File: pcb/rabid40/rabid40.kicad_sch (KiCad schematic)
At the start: 12 parts

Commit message: schematic basics laid down
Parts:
- added D1, D2, D3, D4: 1N4148W, Diode_SMD:D_SOD-123, symbol Diode:1N4148W
- added F1: 500mA, Fuse:Fuse_1206_3216Metric, symbol Device:Polyfuse_Small
- added MX1, MX2, MX3, MX4: MX-NoLED, MX_Alps_Hybrid:MX-1U-NoLED, symbol ai03-mx-alps-hybrid:MX-NoLED
- added R3: 10k, Resistor_SMD:R_0805_2012Metric, symbol Device:R_Small
- added SW1: SW_PUSH, random-keyboard-parts:SKQG-1155865, symbol Keyboard_Symbols:SW_PUSH
- added USB1: Molex-0548190589, random-keyboard-parts:Molex-0548190589, symbol ai03-random-parts:Molex-0548190589
- C1, C2, C3, C4, C5, C6, C7: renamed from C?; footprint (none) -> Capacitor_SMD:C_0805_2012Metric
- R1, R2, R4: renamed from R?; footprint (none) -> Resistor_SMD:R_0805_2012Metric
- Y1: renamed from Y?; footprint (none) -> Crystal:Crystal_SMD_3225-4Pin_3.2x2.5mm
- gave numbers to parts that had none: 1
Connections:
- net +5V: now also F1.2, R3.2
- net GND: now also SW1.1, USB1.1 (GND)
- net D+: now reaches R2.1
- net D+: now also USB1.3 (D+)
- net at U1.13 (~{RESET}): now also R3.1, SW1.2
- net D-: now reaches R1.1
- net D-: now also USB1.4 (D-)
- new net: D2.2 (A), MX2.2 (ROW)
- new net: D4.2 (A), MX4.2 (ROW)
- new net: D1.2 (A), MX1.2 (ROW)
- new net: D3.2 (A), MX3.2 (ROW)
- new net Col0: MX1.1 (COL), MX2.1 (COL)
- new net Col1: MX3.1 (COL), MX4.1 (COL)
- new net Row0: D1.1 (K), D2.1 (K), D3.1 (K), D4.1 (K)
- new net VCC: F1.1, USB1.5 (VBUS)
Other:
- moved on the sheet: C1, C2, C3, C4, C5, C6, C7, R1, R2, R4, U1, Y1

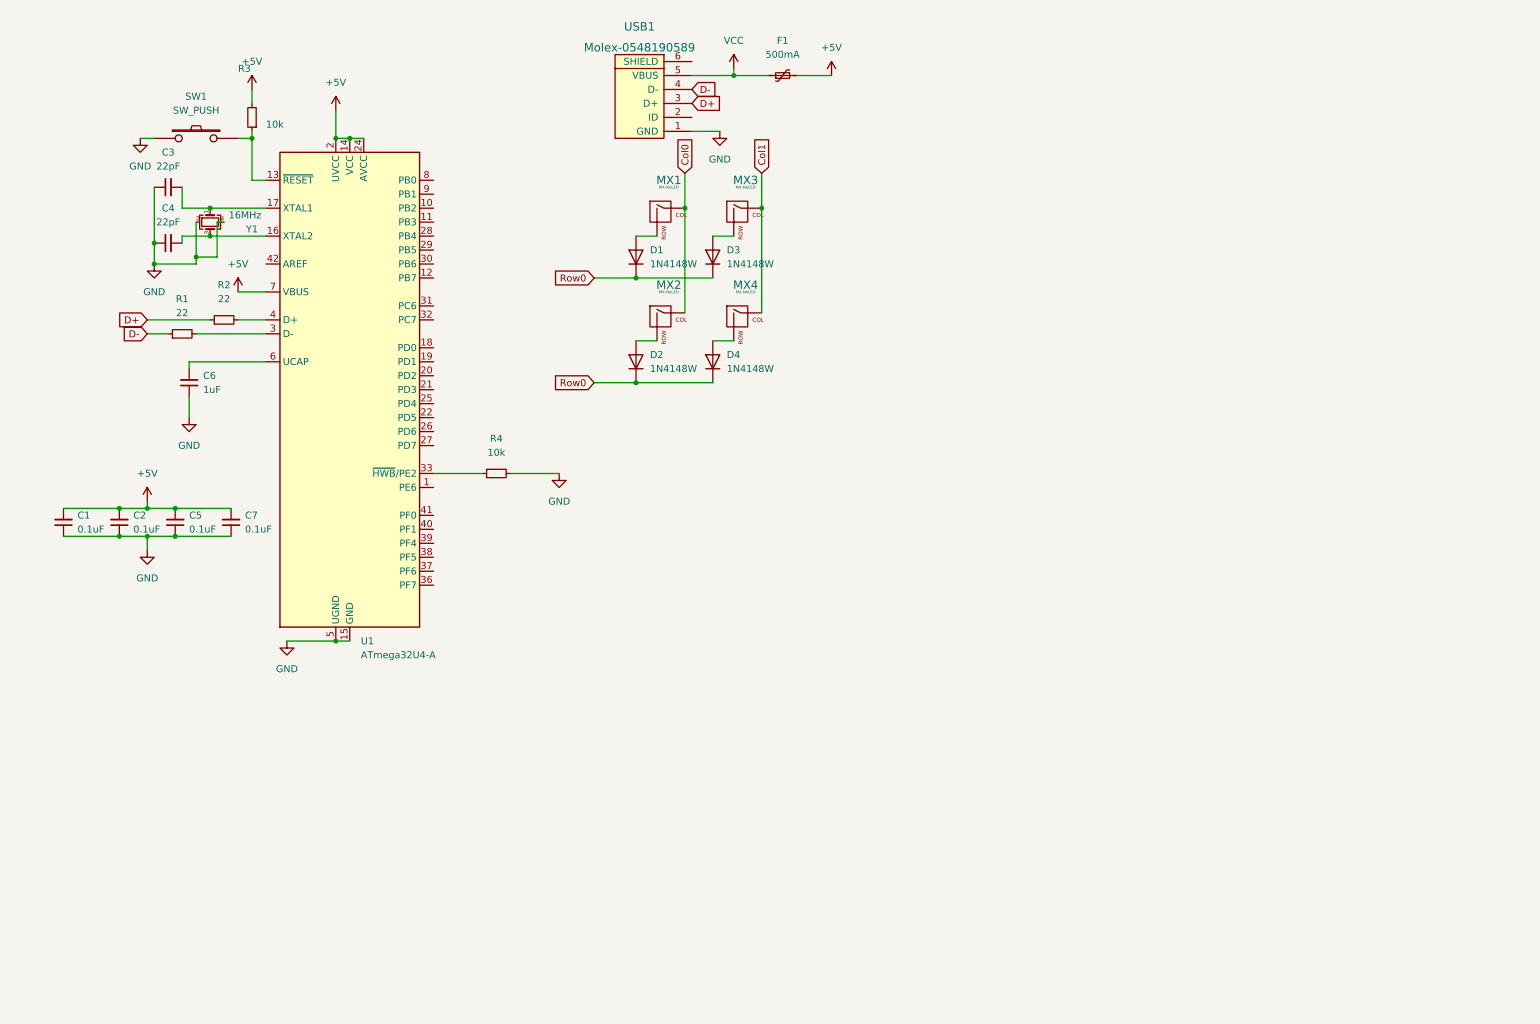
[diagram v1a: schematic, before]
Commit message: all components added for the 40
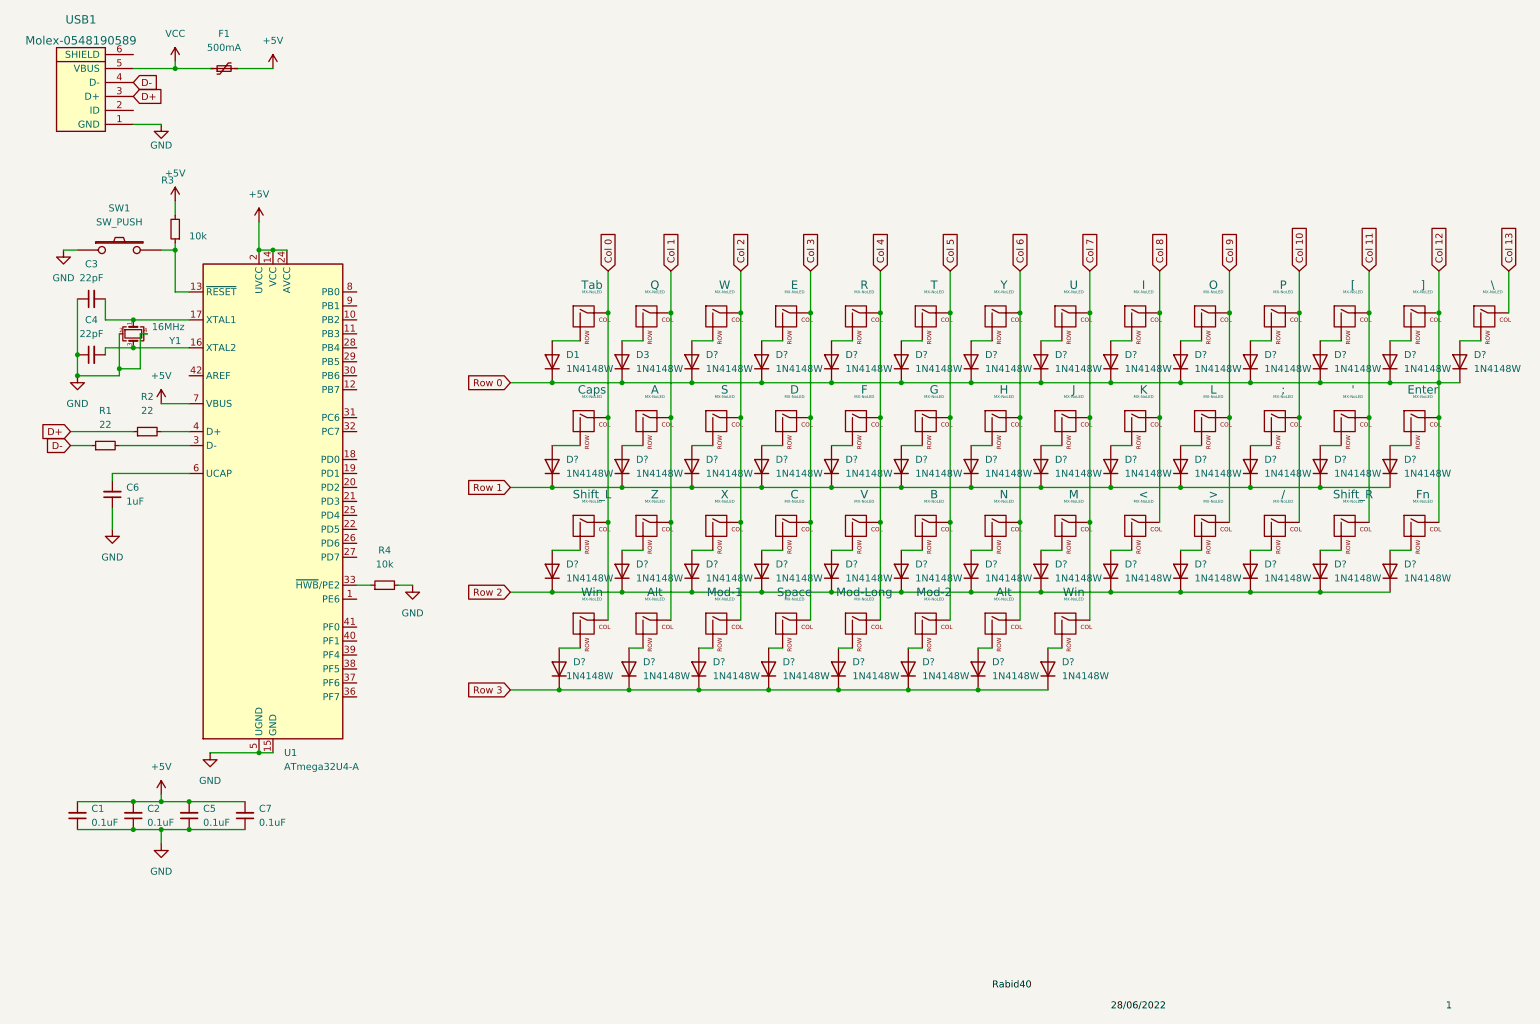
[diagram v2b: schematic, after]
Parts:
- removed D2, D4: 1N4148W, Diode_SMD:D_SOD-123, symbol Diode:1N4148W
- removed MX2, MX4: MX-NoLED, MX_Alps_Hybrid:MX-1U-NoLED, symbol ai03-mx-alps-hybrid:MX-NoLED
- added ', /, ;, <, >, A, Alt (x2), B, C, Caps, D, E, Enter, F, Fn, G, H, I, J, K, L, M, Mod-1, Mod-2, Mod-Long, N, O, P, R, S, Shift_L, Shift_R, Space, T, U, V, W, Win (x2), X, Y, Z, [, \, ]: MX-NoLED, MX_Alps_Hybrid:MX-1U-NoLED, symbol ai03-mx-alps-hybrid:MX-NoLED
- added D? (x46): 1N4148W, Diode_SMD:D_SOD-123, symbol Diode:1N4148W
- renumbered MX3 to Q, MX1 to Tab
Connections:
- net Col0 renamed Col 0
- net Col 0: now also Caps.1 (COL), Shift_L.1 (COL), Win.1 (COL)
- net Col1 renamed Col 1
- net Col 1: now also A.1 (COL), Alt.1 (COL), Z.1 (COL)
- net Row0 renamed Col 12
- net Col 12: now also D?.1 (K), D?.1 (K), D?.1 (K), D?.1 (K), D?.1 (K), D?.1 (K), D?.1 (K), D?.1 (K), D?.1 (K), D?.1 (K), D?.1 (K), D?.1 (K), Enter.1 (COL), Fn.1 (COL), ].1 (COL)
- new net: D?.2 (A), Y.2 (ROW)
- new net: D?.2 (A), U.2 (ROW)
- new net: <.2 (ROW), D?.2 (A)
- new net: D?.2 (A), W.2 (ROW)
- new net: D?.2 (A), G.2 (ROW)
- new net: D?.2 (A), K.2 (ROW)
- new net: D?.2 (A), T.2 (ROW)
- new net: D?.2 (A), P.2 (ROW)
- new net: D?.2 (A), X.2 (ROW)
- new net: B.2 (ROW), D?.2 (A)
- new net: D?.2 (A), J.2 (ROW)
- new net: D?.2 (A), O.2 (ROW)
- new net: A.2 (ROW), D?.2 (A)
- new net: ;.2 (ROW), D?.2 (A)
- new net: D?.2 (A), ].2 (ROW)
- new net: D?.2 (A), E.2 (ROW)
- new net: >.2 (ROW), D?.2 (A)
- new net: Alt.2 (ROW), D?.2 (A) (x2)
- new net: D?.2 (A), Mod-1.2 (ROW)
- new net: D?.2 (A), V.2 (ROW)
- new net: D?.2 (A), M.2 (ROW)
- new net: D?.2 (A), Enter.2 (ROW)
- new net: D?.2 (A), I.2 (ROW)
- new net: D?.2 (A), S.2 (ROW)
- new net: D?.2 (A), Fn.2 (ROW)
- new net: D?.2 (A), [.2 (ROW)
- new net: D?.2 (A), L.2 (ROW)
- new net: D?.2 (A), Z.2 (ROW)
- new net: D?.2 (A), Win.2 (ROW) (x2)
- new net: '.2 (ROW), D?.2 (A)
- new net: Caps.2 (ROW), D?.2 (A)
- new net: /.2 (ROW), D?.2 (A)
- new net: D?.2 (A), \.2 (ROW)
- new net: D?.2 (A), Space.2 (ROW)
- new net: D?.2 (A), Mod-2.2 (ROW)
- new net: C.2 (ROW), D?.2 (A)
- new net: D?.2 (A), R.2 (ROW)
- new net: D.2 (ROW), D?.2 (A)
- new net: D?.2 (A), F.2 (ROW)
- new net: D?.2 (A), N.2 (ROW)
- new net: D?.2 (A), Shift_R.2 (ROW)
- new net: D?.2 (A), Shift_L.2 (ROW)
- new net: D?.2 (A), H.2 (ROW)
- new net: D?.2 (A), Mod-Long.2 (ROW)
- new net Col 10: /.1 (COL), ;.1 (COL), P.1 (COL)
- new net Col 11: '.1 (COL), Shift_R.1 (COL), [.1 (COL)
- new net Col 13: \.1 (COL)
- new net Col 2: Mod-1.1 (COL), S.1 (COL), W.1 (COL), X.1 (COL)
- new net Col 3: C.1 (COL), D.1 (COL), E.1 (COL), Space.1 (COL)
- new net Col 4: F.1 (COL), Mod-Long.1 (COL), R.1 (COL), V.1 (COL)
- new net Col 5: B.1 (COL), G.1 (COL), Mod-2.1 (COL), T.1 (COL)
- new net Col 6: Alt.1 (COL), H.1 (COL), N.1 (COL), Y.1 (COL)
- new net Col 7: J.1 (COL), M.1 (COL), U.1 (COL), Win.1 (COL)
- new net Col 8: <.1 (COL), I.1 (COL), K.1 (COL)
- new net Col 9: >.1 (COL), L.1 (COL), O.1 (COL)
- new net Row 1: D?.1 (K), D?.1 (K), D?.1 (K), D?.1 (K), D?.1 (K), D?.1 (K), D?.1 (K), D?.1 (K), D?.1 (K), D?.1 (K), D?.1 (K), D?.1 (K), D?.1 (K)
- new net Row 2: D?.1 (K), D?.1 (K), D?.1 (K), D?.1 (K), D?.1 (K), D?.1 (K), D?.1 (K), D?.1 (K), D?.1 (K), D?.1 (K), D?.1 (K), D?.1 (K), D?.1 (K)
- new net Row 3: D?.1 (K), D?.1 (K), D?.1 (K), D?.1 (K), D?.1 (K), D?.1 (K), D?.1 (K), D?.1 (K)
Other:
- moved on the sheet: C1, C2, C3, C4, C5, C6, C7, D1, D3, F1, Q, R1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

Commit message: basic routing
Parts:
- Caps1: renamed from Caps; footprint MX_Alps_Hybrid:MX-1U-NoLED -> MX_Alps_Hybrid:MX-1.25U
- gave numbers to parts that had none: 46
- renumbered ' to '1, / to /1, ; to ;1, < to <1, > to >1, A to A1, Alt to Alt1, Alt to Alt2, B to B1, C to C8, D to D17, E to E1, Enter to Enter1, F to F2, Fn to Fn1, G to G1, H to H1, I to I1, J to J1, K to K1, L to L1, M to M1, Mod-Long to Mod-Long1, N to N1, O to O1, P to P1, Q to Q1, R to R5, S to S1, Shift_L to Shift_L1, Shift_R to Shift_R1, Space to Space1, T to T1, Tab to Tab1, U to U2, V to V1, W to W1, Win to Win1, Win to Win2, X to X1, Y to Y2, Z to Z1, [ to [1, \ to \1, ] to ]1

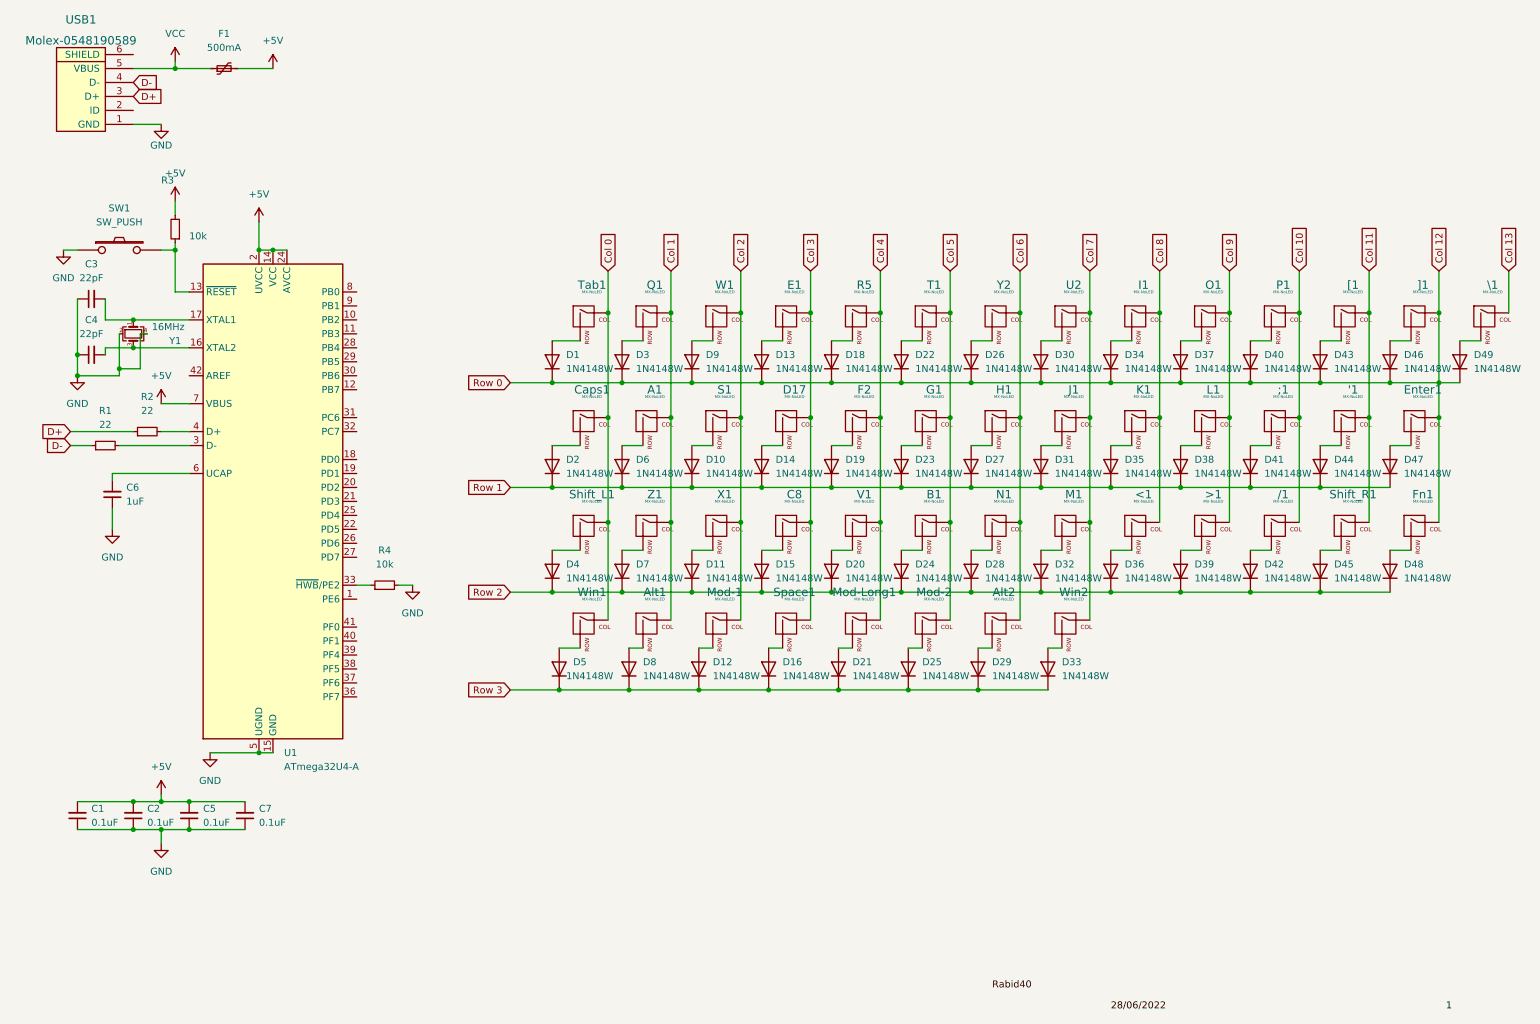
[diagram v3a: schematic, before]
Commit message: added multilayout support to schematic
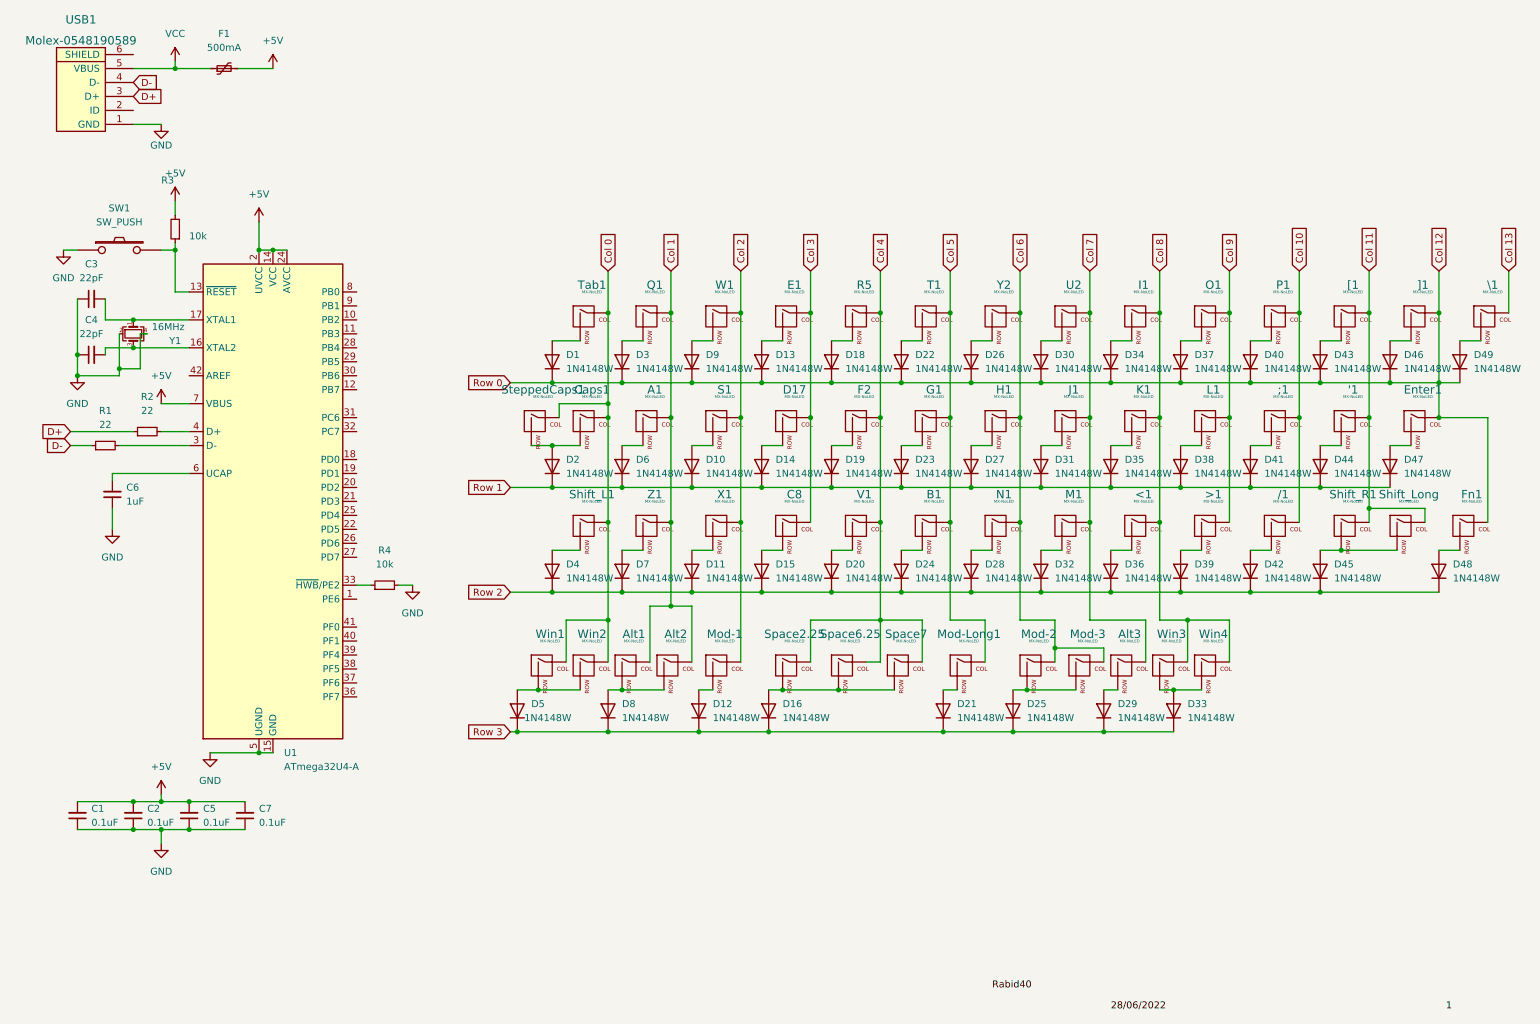
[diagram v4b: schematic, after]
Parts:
- added Alt2, Win2, Win3: MX-NoLED, MX_Alps_Hybrid:MX-1.25U, symbol ai03-mx-alps-hybrid:MX-NoLED
- added Mod-3: MX-NoLED, MX_Alps_Hybrid:MX-1U-NoLED, symbol ai03-mx-alps-hybrid:MX-NoLED
- added Shift_Long: MX-NoLED, MX_Alps_Hybrid:MX-2.75U, symbol ai03-mx-alps-hybrid:MX-NoLED
- added Space6.25: MX-NoLED, MX_Alps_Hybrid:MX-6.25U, symbol ai03-mx-alps-hybrid:MX-NoLED
- added Space7: MX-NoLED, MX_Alps_Hybrid:MX-7U, symbol ai03-mx-alps-hybrid:MX-NoLED
- added SteppedCaps1: MX-NoLED, MX_Alps_Hybrid:MX-1U, symbol ai03-mx-alps-hybrid:MX-NoLED
- Alt1, Tab1, \1: footprint MX_Alps_Hybrid:MX-1U-NoLED -> MX_Alps_Hybrid:MX-1.5U
- Alt3: renamed from Alt2; footprint MX_Alps_Hybrid:MX-1U-NoLED -> MX_Alps_Hybrid:MX-1.5U
- Caps1: footprint MX_Alps_Hybrid:MX-1.25U -> MX_Alps_Hybrid:MX-1.75U
- Enter1, Shift_L1: footprint MX_Alps_Hybrid:MX-1U-NoLED -> MX_Alps_Hybrid:MX-2.25U
- Mod-Long1: footprint MX_Alps_Hybrid:MX-1U-NoLED -> MX_Alps_Hybrid:MX-2.75U
- Shift_R1: footprint MX_Alps_Hybrid:MX-1U-NoLED -> MX_Alps_Hybrid:MX-1.75U
- Space2.25: renamed from Space1; footprint MX_Alps_Hybrid:MX-1U-NoLED -> MX_Alps_Hybrid:MX-2.25U
- renumbered Win2 to Win4
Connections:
- net Col 0: now also SteppedCaps1.1 (COL), Win2.1 (COL)
- net Col 1: now also Alt2.1 (COL)
- net Col 11: now also Shift_Long.1 (COL)
- net Col 3: no longer Space2.25.1 (COL)
- net Col 4: now also Space2.25.1 (COL), Space6.25.1 (COL), Space7.1 (COL); no longer Mod-Long1.1 (COL)
- net Col 5: now also Mod-Long1.1 (COL); no longer Mod-2.1 (COL)
- net Col 6: now also Mod-2.1 (COL), Mod-3.1 (COL); no longer Alt3.1 (COL)
- net Col 7: now also Alt3.1 (COL); no longer Win4.1 (COL)
- net Col 8: now also Win4.1 (COL), Win3.1 (COL)
- net at Alt1.2 (ROW), D8.2 (A): now also Alt2.2 (ROW)
- net at D33.2 (A), Win4.2 (ROW): now also Win3.2 (ROW)
- net at Caps1.2 (ROW), D2.2 (A): now also SteppedCaps1.2 (ROW)
- net at D16.2 (A), Space2.25.2 (ROW): now also Space6.25.2 (ROW), Space7.2 (ROW)
- net at D25.2 (A), Mod-2.2 (ROW): now also Mod-3.2 (ROW)
- net at D5.2 (A), Win1.2 (ROW): now also Win2.2 (ROW)
- net at D45.2 (A), Shift_R1.2 (ROW): now also Shift_Long.2 (ROW)
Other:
- moved on the sheet: Alt1, Alt3, D12, D16, D21, D25, D29, D33, D48, D5, D8, Fn1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

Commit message: more switches aligned
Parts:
- '1, /1, ;1, <1, >1, A1, B1, C8, D17, E1, F2, Fn1, G1, H1, I1, J1, K1, L1, M1, Mod-1, Mod-2, Mod-3, N1, O1, P1, Q1, R5, S1, T1, U2, V1, W1, Win1, Win4, X1, Y2, Z1, [1, ]1: footprint MX_Alps_Hybrid:MX-1U-NoLED -> MX_Alps_Hybrid:MX-1U
- renumbered Shift_Long to Shift_Long1
